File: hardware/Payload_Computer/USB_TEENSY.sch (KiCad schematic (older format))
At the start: 7 parts, among them J2 USB_B_Micro, U801 MKL02Z32VFG4

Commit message: minor changes
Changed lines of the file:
@@
 $Descr A4 11693 8268
 encoding utf-8
-Sheet 8 21
+Sheet 12 21
 Title ""
 Date ""
@@
 AR Path="/5F86D5A7/5F87457D" Ref="J2"  Part="1"
 AR Path="/60289E3E/5F87457D" Ref="J1801"  Part="1"
-F 0 "J2" H 3207 3967 50  0000 C CNN
+F 0 "J1801" H 3207 3967 50  0000 C CNN
 F 1 "USB_B_Micro" H 3207 3876 50  0000 C CNN
 F 2 "" H 3300 3450 50  0001 C CNN
@@
 AR Path="/5F86D5A7/5F874583" Ref="F2"  Part="1"
 AR Path="/60289E3E/5F874583" Ref="F1801"  Part="1"
-F 0 "F2" V 3653 3300 50  0000 C CNN
+F 0 "F1801" V 3653 3300 50  0000 C CNN
 F 1 "Fuse" V 3744 3300 50  0000 C CNN
 F 2 "Fuse:Fuse_0603_1608Metric_Pad1.05x0.95mm_HandSolder" V 3780 3300 50  0001 C CNN
@@
 AR Path="/5F86D5A7/5F87458A" Ref="C10"  Part="1"
 AR Path="/60289E3E/5F87458A" Ref="C1801"  Part="1"
-F 0 "C10" H 3482 2854 50  0000 R CNN
+F 0 "C1801" H 3482 2854 50  0000 R CNN
 F 1 "10nF" H 3482 2945 50  0000 R CNN
 F 2 "Capacitor_SMD:C_0603_1608Metric_Pad1.08x0.95mm_HandSolder" H 3638 2750 50  0001 C CNN
@@
 AR Path="/5F86D5A7/5F874593" Ref="#PWR0117"  Part="1"
 AR Path="/60289E3E/5F874593" Ref="#PWR01802"  Part="1"
-F 0 "#PWR0117" H 3600 2300 50  0001 C CNN
+F 0 "#PWR01802" H 3600 2300 50  0001 C CNN
 F 1 "GND" H 3605 2377 50  0000 C CNN
 F 2 "" H 3600 2550 50  0001 C CNN
@@
 AR Path="/5F86D5A7/5F87459A" Ref="FB2"  Part="1"
 AR Path="/60289E3E/5F87459A" Ref="FB1801"  Part="1"
-F 0 "FB2" V 4163 3300 50  0000 C CNN
+F 0 "FB1801" V 4163 3300 50  0000 C CNN
 F 1 "600 OHM" V 4254 3300 50  0000 C CNN
 F 2 "Capacitor_SMD:C_0603_1608Metric_Pad1.08x0.95mm_HandSolder" V 4330 3300 50  0001 C CNN
@@
 AR Path="/5F86D5A7/5F8745A8" Ref="#PWR0119"  Part="1"
 AR Path="/60289E3E/5F8745A8" Ref="#PWR01801"  Part="1"
-F 0 "#PWR0119" H 3150 3900 50  0001 C CNN
+F 0 "#PWR01801" H 3150 3900 50  0001 C CNN
 F 1 "GND" H 3155 3977 50  0000 C CNN
 F 2 "" H 3150 4150 50  0001 C CNN
@@
 AR Path="/5F86D5A7/5FAFD9D4" Ref="R801"  Part="1"
 AR Path="/60289E3E/5FAFD9D4" Ref="R1801"  Part="1"
-F 0 "R801" V 4350 3600 50  0000 C CNN
+F 0 "R1801" V 4350 3600 50  0000 C CNN
 F 1 "33 OHM" V 4250 3600 50  0000 C CNN
 F 2 "Resistor_SMD:R_0603_1608Metric_Pad0.98x0.95mm_HandSolder" V 4140 3590 50  0001 C CNN
@@
 AR Path="/5F86D5A7/5FAFE37D" Ref="R802"  Part="1"
 AR Path="/60289E3E/5FAFE37D" Ref="R1802"  Part="1"
-F 0 "R802" V 4300 3700 50  0000 C CNN
+F 0 "R1802" V 4300 3700 50  0000 C CNN
 F 1 "33 OHM" V 4300 3500 50  0000 C CNN
 F 2 "Resistor_SMD:R_0603_1608Metric_Pad0.98x0.95mm_HandSolder" V 4440 3490 50  0001 C CNN
@@
 AR Path="/5F86D5A7/5FB00371" Ref="U801"  Part="1"
 AR Path="/60289E3E/5FB00371" Ref="U1801"  Part="1"
-F 0 "U801" H 8350 5400 50  0000 C CNN
+F 0 "U1801" H 8350 5400 50  0000 C CNN
 F 1 "MKL02Z32VFG4" H 8350 5300 50  0000 C CNN
 F 2 "Package_DFN_QFN:QFN-16-1EP_3x3mm_P0.5mm_EP1.9x1.9mm" H 8500 1975 50  0001 L TNN
@@
 AR Path="/5F86D5A7/5FB010A8" Ref="#PWR0802"  Part="1"
 AR Path="/60289E3E/5FB010A8" Ref="#PWR01804"  Part="1"
-F 0 "#PWR0802" H 8350 1450 50  0001 C CNN
+F 0 "#PWR01804" H 8350 1450 50  0001 C CNN
 F 1 "+3.3V" H 8365 1773 50  0000 C CNN
 F 2 "" H 8350 1600 50  0001 C CNN
@@
 AR Path="/5F86D5A7/5FB025B3" Ref="#PWR0803"  Part="1"
 AR Path="/60289E3E/5FB025B3" Ref="#PWR01805"  Part="1"
-F 0 "#PWR0803" H 8350 4650 50  0001 C CNN
+F 0 "#PWR01805" H 8350 4650 50  0001 C CNN
 F 1 "GND" H 8355 4727 50  0000 C CNN
 F 2 "" H 8350 4900 50  0001 C CNN
@@
 AR Path="/5F86D5A7/5FC29DFB" Ref="#PWR0801"  Part="1"
 AR Path="/60289E3E/5FC29DFB" Ref="#PWR01803"  Part="1"
-F 0 "#PWR0801" H 4850 3150 50  0001 C CNN
+F 0 "#PWR01803" H 4850 3150 50  0001 C CNN
 F 1 "VBUS" V 4865 3428 50  0000 L CNN
 F 2 "" H 4850 3300 50  0001 C CNN

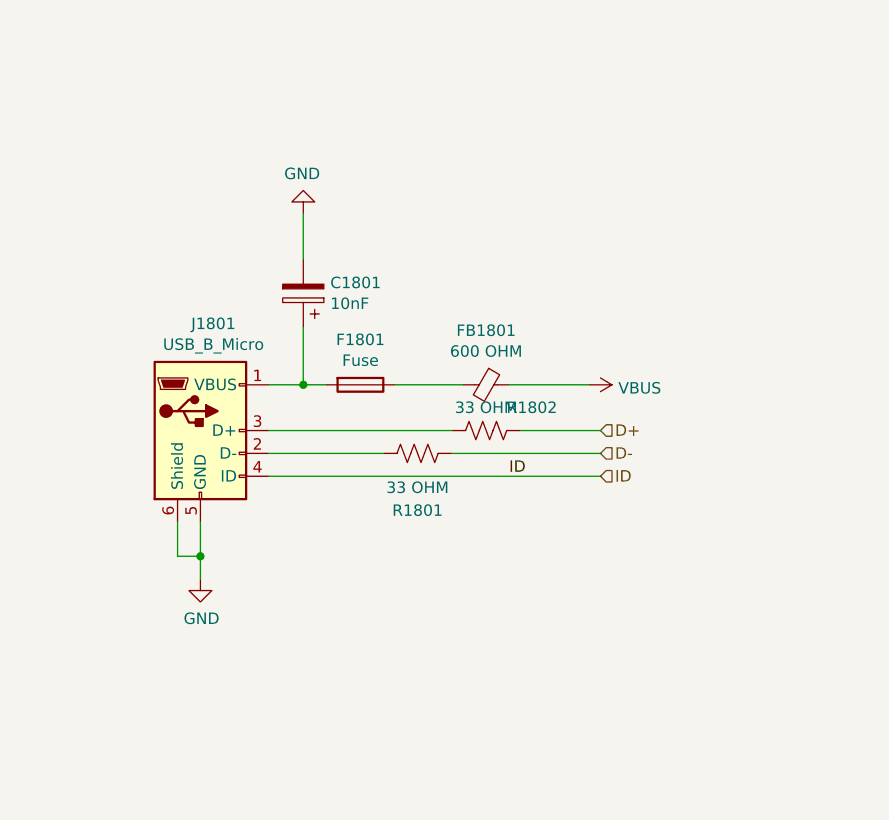
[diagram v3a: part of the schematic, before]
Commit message: Added last footprints and started routing
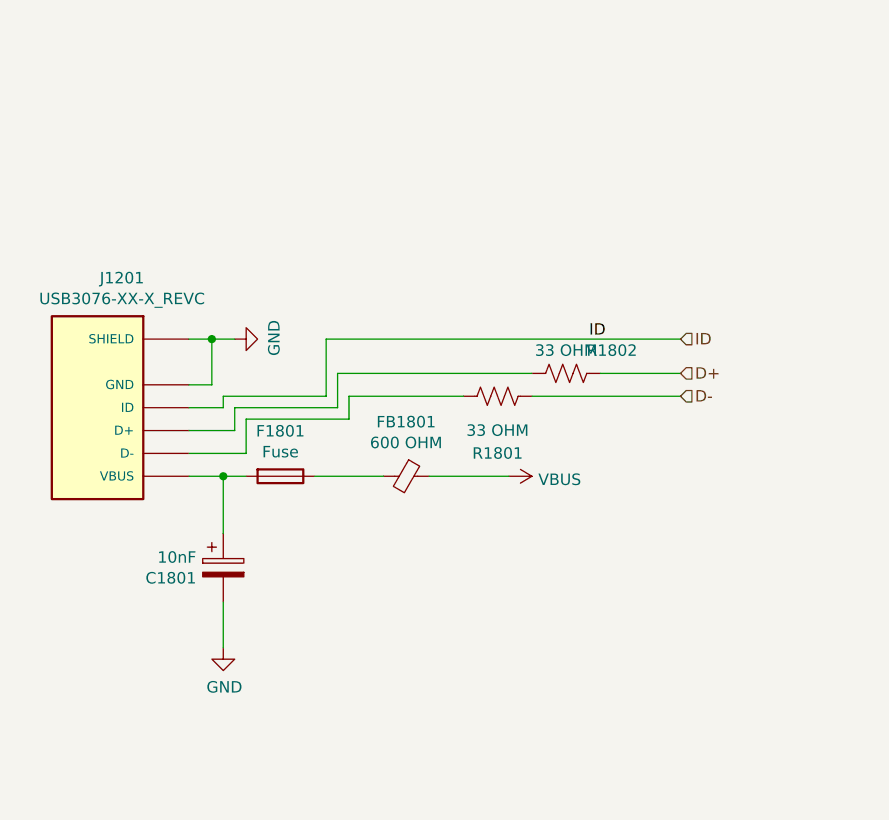
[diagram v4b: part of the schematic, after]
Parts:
- removed J2: USB_B_Micro, symbol Symbols:USB_B_Micro
- added J1201: USB3076-XX-X_REVC, USB3076-XX-X_REVC:GCT_USB3076-XX-X_REVC, symbol USB3076-XX-X_REVC:USB3076-XX-X_REVC
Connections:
- wire segments 27 -> 39
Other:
- moved on the sheet: C1801, F1801, FB1801, R1801, R1802
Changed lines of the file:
@@
 $Descr A4 11693 8268
 encoding utf-8
-Sheet 12 21
+Sheet 8 21
 Title ""
 Date ""
@@
 $EndDescr
 $Comp
-L Symbols:USB_B_Micro J2
-U 1 1 5F87457D
-P 3150 3500
-AR Path="/5F86D5A7/5F87457D" Ref="J2"  Part="1"
-AR Path="/60289E3E/5F87457D" Ref="J1801"  Part="1"
-F 0 "J1801" H 3207 3967 50  0000 C CNN
-F 1 "USB_B_Micro" H 3207 3876 50  0000 C CNN
-F 2 "" H 3300 3450 50  0001 C CNN
-F 3 "~" H 3300 3450 50  0001 C CNN
-	1    3150 3500
-	1    0    0    -1
-$EndComp
-$Comp
 L Device:Fuse F2
 U 1 1 5F874583
-P 3850 3300
+P 3500 3700
 AR Path="/5F86D5A7/5F874583" Ref="F2"  Part="1"
 AR Path="/60289E3E/5F874583" Ref="F1801"  Part="1"
-F 0 "F1801" V 3653 3300 50  0000 C CNN
-F 1 "Fuse" V 3744 3300 50  0000 C CNN
-F 2 "Fuse:Fuse_0603_1608Metric_Pad1.05x0.95mm_HandSolder" V 3780 3300 50  0001 C CNN
-F 3 "~" H 3850 3300 50  0001 C CNN
-	1    3850 3300
-	0    1    1    0
-$EndComp
-Wire Wire Line
-	3450 3300 3600 3300
+F 0 "F1801" V 3303 3700 50  0000 C CNN
+F 1 "Fuse" V 3394 3700 50  0000 C CNN
+F 2 "Fuse:Fuse_0603_1608Metric_Pad1.05x0.95mm_HandSolder" V 3430 3700 50  0001 C CNN
+F 3 "~" H 3500 3700 50  0001 C CNN
+	1    3500 3700
+	0    1    1    0
+$EndComp
+Wire Wire Line
+	3100 3700 3250 3700
 $Comp
 L Device:CP C10
 U 1 1 5F87458A
-P 3600 2900
+P 3250 4100
 AR Path="/5F86D5A7/5F87458A" Ref="C10"  Part="1"
 AR Path="/60289E3E/5F87458A" Ref="C1801"  Part="1"
-F 0 "C1801" H 3482 2854 50  0000 R CNN
-F 1 "10nF" H 3482 2945 50  0000 R CNN
-F 2 "Capacitor_SMD:C_0603_1608Metric_Pad1.08x0.95mm_HandSolder" H 3638 2750 50  0001 C CNN
-F 3 "~" H 3600 2900 50  0001 C CNN
-	1    3600 2900
-	-1   0    0    1
-$EndComp
-Wire Wire Line
-	3600 3050 3600 3300
-Connection ~ 3600 3300
-Wire Wire Line
-	3600 3300 3700 3300
+F 0 "C1801" H 3132 4054 50  0000 R CNN
+F 1 "10nF" H 3132 4145 50  0000 R CNN
+F 2 "Capacitor_SMD:C_0603_1608Metric_Pad1.08x0.95mm_HandSolder" H 3288 3950 50  0001 C CNN
+F 3 "~" H 3250 4100 50  0001 C CNN
+	1    3250 4100
+	1    0    0    -1
+$EndComp
+Wire Wire Line
+	3250 3950 3250 3700
+Connection ~ 3250 3700
+Wire Wire Line
+	3250 3700 3350 3700
 $Comp
 L power:GND #PWR0117
 U 1 1 5F874593
-P 3600 2550
+P 3250 4450
 AR Path="/5F86D5A7/5F874593" Ref="#PWR0117"  Part="1"
 AR Path="/60289E3E/5F874593" Ref="#PWR01802"  Part="1"
-F 0 "#PWR01802" H 3600 2300 50  0001 C CNN
-F 1 "GND" H 3605 2377 50  0000 C CNN
-F 2 "" H 3600 2550 50  0001 C CNN
-F 3 "" H 3600 2550 50  0001 C CNN
-	1    3600 2550
-	-1   0    0    1
-$EndComp
-Wire Wire Line
-	3600 2750 3600 2550
+F 0 "#PWR01802" H 3250 4200 50  0001 C CNN
+F 1 "GND" H 3255 4277 50  0000 C CNN
+F 2 "" H 3250 4450 50  0001 C CNN
+F 3 "" H 3250 4450 50  0001 C CNN
+	1    3250 4450
+	1    0    0    -1
+$EndComp
+Wire Wire Line
+	3250 4250 3250 4450
 $Comp
 L Device:Ferrite_Bead_Small FB2
 U 1 1 5F87459A
-P 4400 3300
+P 4050 3700
 AR Path="/5F86D5A7/5F87459A" Ref="FB2"  Part="1"
 AR Path="/60289E3E/5F87459A" Ref="FB1801"  Part="1"
-F 0 "FB1801" V 4163 3300 50  0000 C CNN
-F 1 "600 OHM" V 4254 3300 50  0000 C CNN
-F 2 "Capacitor_SMD:C_0603_1608Metric_Pad1.08x0.95mm_HandSolder" V 4330 3300 50  0001 C CNN
-F 3 "~" H 4400 3300 50  0001 C CNN
-	1    4400 3300
-	0    1    1    0
-$EndComp
-Wire Wire Line
-	4000 3300 4300 3300
-Wire Wire Line
-	4500 3300 4850 3300
-$Comp
-L power:GND #PWR0119
-U 1 1 5F8745A8
-P 3150 4150
-AR Path="/5F86D5A7/5F8745A8" Ref="#PWR0119"  Part="1"
-AR Path="/60289E3E/5F8745A8" Ref="#PWR01801"  Part="1"
-F 0 "#PWR01801" H 3150 3900 50  0001 C CNN
-F 1 "GND" H 3155 3977 50  0000 C CNN
-F 2 "" H 3150 4150 50  0001 C CNN
-F 3 "" H 3150 4150 50  0001 C CNN
-	1    3150 4150
-	1    0    0    -1
-$EndComp
-Wire Wire Line
-	3150 3900 3150 4050
-Wire Wire Line
-	3050 3900 3050 4050
-Wire Wire Line
-	3050 4050 3150 4050
-Connection ~ 3150 4050
-Wire Wire Line
-	3150 4050 3150 4150
-Wire Wire Line
-	3450 3600 3950 3600
+F 0 "FB1801" V 3813 3700 50  0000 C CNN
+F 1 "600 OHM" V 3904 3700 50  0000 C CNN
+F 2 "Capacitor_SMD:C_0603_1608Metric_Pad1.08x0.95mm_HandSolder" V 3980 3700 50  0001 C CNN
+F 3 "~" H 4050 3700 50  0001 C CNN
+	1    4050 3700
+	0    1    1    0
+$EndComp
+Wire Wire Line
+	3650 3700 3950 3700
+Wire Wire Line
+	4150 3700 4500 3700
+Wire Wire Line
+	3800 3350 4300 3350
 $Comp
 L Device:R_US R801
 U 1 1 5FAFD9D4
-P 4100 3600
+P 4450 3350
 AR Path="/5F86D5A7/5FAFD9D4" Ref="R801"  Part="1"
 AR Path="/60289E3E/5FAFD9D4" Ref="R1801"  Part="1"
-F 0 "R1801" V 4350 3600 50  0000 C CNN
-F 1 "33 OHM" V 4250 3600 50  0000 C CNN
-F 2 "Resistor_SMD:R_0603_1608Metric_Pad0.98x0.95mm_HandSolder" V 4140 3590 50  0001 C CNN
-F 3 "~" H 4100 3600 50  0001 C CNN
-	1    4100 3600
+F 0 "R1801" V 4700 3350 50  0000 C CNN
+F 1 "33 OHM" V 4600 3350 50  0000 C CNN
+F 2 "Resistor_SMD:R_0603_1608Metric_Pad0.98x0.95mm_HandSolder" V 4490 3340 50  0001 C CNN
+F 3 "~" H 4450 3350 50  0001 C CNN
+	1    4450 3350
 	0    1    1    0
 $EndComp
@@
 L Device:R_US R802
 U 1 1 5FAFE37D
-P 4400 3500
+P 4750 3250
 AR Path="/5F86D5A7/5FAFE37D" Ref="R802"  Part="1"
 AR Path="/60289E3E/5FAFE37D" Ref="R1802"  Part="1"
-F 0 "R1802" V 4300 3700 50  0000 C CNN
-F 1 "33 OHM" V 4300 3500 50  0000 C CNN
-F 2 "Resistor_SMD:R_0603_1608Metric_Pad0.98x0.95mm_HandSolder" V 4440 3490 50  0001 C CNN
-F 3 "~" H 4400 3500 50  0001 C CNN
-	1    4400 3500
-	0    1    1    0
-$EndComp
-Wire Wire Line
-	3450 3500 4250 3500
-Wire Wire Line
-	4250 3600 4900 3600
-Wire Wire Line
-	4550 3500 4900 3500
-Text HLabel 4900 3500 2    50   Input ~ 0
+F 0 "R1802" V 4650 3450 50  0000 C CNN
+F 1 "33 OHM" V 4650 3250 50  0000 C CNN
+F 2 "Resistor_SMD:R_0603_1608Metric_Pad0.98x0.95mm_HandSolder" V 4790 3240 50  0001 C CNN
+F 3 "~" H 4750 3250 50  0001 C CNN
+	1    4750 3250
+	0    1    1    0
+$EndComp
+Wire Wire Line
+	4600 3350 5250 3350
+Wire Wire Line
+	4900 3250 5250 3250
+Text HLabel 5250 3250 2    50   Input ~ 0
 D+
-Text HLabel 4900 3600 2    50   Input ~ 0
+Text HLabel 5250 3350 2    50   Input ~ 0
 D-
-Wire Wire Line
-	3450 3700 4900 3700
-Text HLabel 4900 3700 2    50   Input ~ 0
+Text HLabel 5250 3100 2    50   Input ~ 0
 ID
 $Comp
@@
 Wire Wire Line
 	8350 1600 8350 1800
-Text Label 4500 3700 0    50   ~ 0
+Text Label 4850 3100 0    50   ~ 0
 ID
 Wire Wire Line
@@
 L power:VBUS #PWR0801
 U 1 1 5FC29DFB
-P 4850 3300
+P 4500 3700
 AR Path="/5F86D5A7/5FC29DFB" Ref="#PWR0801"  Part="1"
 AR Path="/60289E3E/5FC29DFB" Ref="#PWR01803"  Part="1"
-F 0 "#PWR01803" H 4850 3150 50  0001 C CNN
-F 1 "VBUS" V 4865 3428 50  0000 L CNN
-F 2 "" H 4850 3300 50  0001 C CNN
-F 3 "" H 4850 3300 50  0001 C CNN
-	1    4850 3300
-	0    1    1    0
-$EndComp
+F 0 "#PWR01803" H 4500 3550 50  0001 C CNN
+F 1 "VBUS" V 4515 3828 50  0000 L CNN
+F 2 "" H 4500 3700 50  0001 C CNN
+F 3 "" H 4500 3700 50  0001 C CNN
+	1    4500 3700
+	0    1    1    0
+$EndComp
+$Comp
+L USB3076-XX-X_REVC:USB3076-XX-X_REVC J1201
+U 1 1 603CD396
+P 2700 3400
+AR Path="/60289E3E/603CD396" Ref="J1201"  Part="1"
+AR Path="/5F86D5A7/603CD396" Ref="J801"  Part="1"
+F 0 "J1201" H 2593 2833 50  0000 C CNN
+F 1 "USB3076-XX-X_REVC" H 2593 2924 50  0000 C CNN
+F 2 "USB3076-XX-X_REVC:GCT_USB3076-XX-X_REVC" H 2700 3400 50  0001 L BNN
+F 3 "" H 2700 3400 50  0001 L BNN
+F 4 "GCT" H 2700 3400 50  0001 L BNN "MANUFACTURER"
+	1    2700 3400
+	-1   0    0    1
+$EndComp
+$Comp
+L power:GND #PWR0114
+U 1 1 603D5B73
+P 3300 3100
+AR Path="/5F86D5A7/603D5B73" Ref="#PWR0114"  Part="1"
+AR Path="/60289E3E/603D5B73" Ref="#PWR0115"  Part="1"
+F 0 "#PWR0115" H 3300 2850 50  0001 C CNN
+F 1 "GND" H 3305 2927 50  0000 C CNN
+F 2 "" H 3300 3100 50  0001 C CNN
+F 3 "" H 3300 3100 50  0001 C CNN
+	1    3300 3100
+	0    -1   -1   0
+$EndComp
+Wire Wire Line
+	3100 3100 3200 3100
+Wire Wire Line
+	3100 3300 3200 3300
+Wire Wire Line
+	3200 3300 3200 3100
+Connection ~ 3200 3100
+Wire Wire Line
+	3200 3100 3300 3100
+Wire Wire Line
+	3100 3600 3350 3600
+Wire Wire Line
+	3350 3600 3350 3450
+Wire Wire Line
+	3350 3450 3800 3450
+Wire Wire Line
+	3800 3450 3800 3350
+Wire Wire Line
+	3100 3500 3300 3500
+Wire Wire Line
+	3300 3500 3300 3400
+Wire Wire Line
+	3300 3400 3750 3400
+Wire Wire Line
+	3750 3400 3750 3250
+Wire Wire Line
+	3750 3250 4600 3250
+Wire Wire Line
+	3100 3400 3250 3400
+Wire Wire Line
+	3250 3400 3250 3350
+Wire Wire Line
+	3250 3350 3700 3350
+Wire Wire Line
+	3700 3350 3700 3100
+Wire Wire Line
+	3700 3100 5250 3100
 $EndSCHEMATC
